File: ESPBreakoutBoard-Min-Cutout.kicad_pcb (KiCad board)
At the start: 2 copper layers, 27.5 x 32.3 mm, 15 parts, among them J1 Screw_Terminal_01x02, J2 Conn_01x09_Male, J3 Conn_01x09_Male, U1 AMS1117-3.3, U2 ESP-07

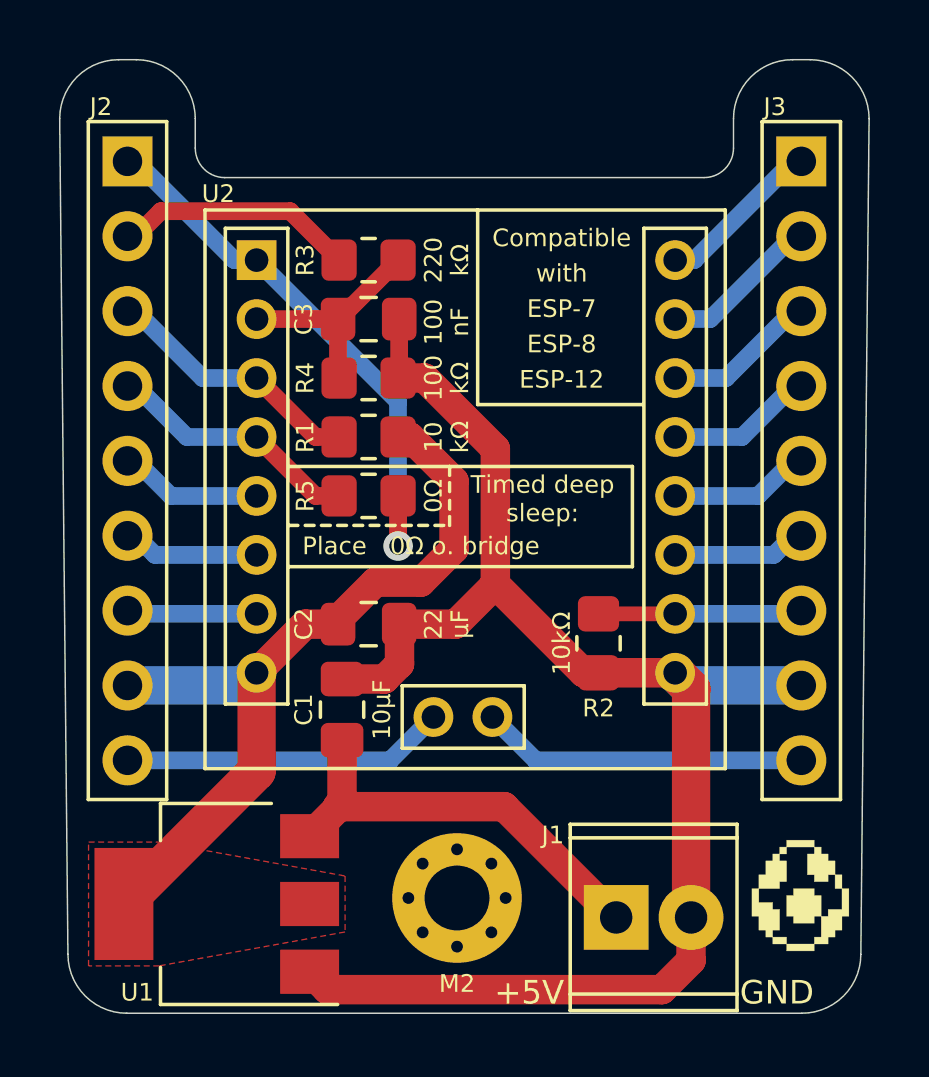
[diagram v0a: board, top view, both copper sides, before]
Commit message: v4r3: Added gerbers, fixed odd edge cuts
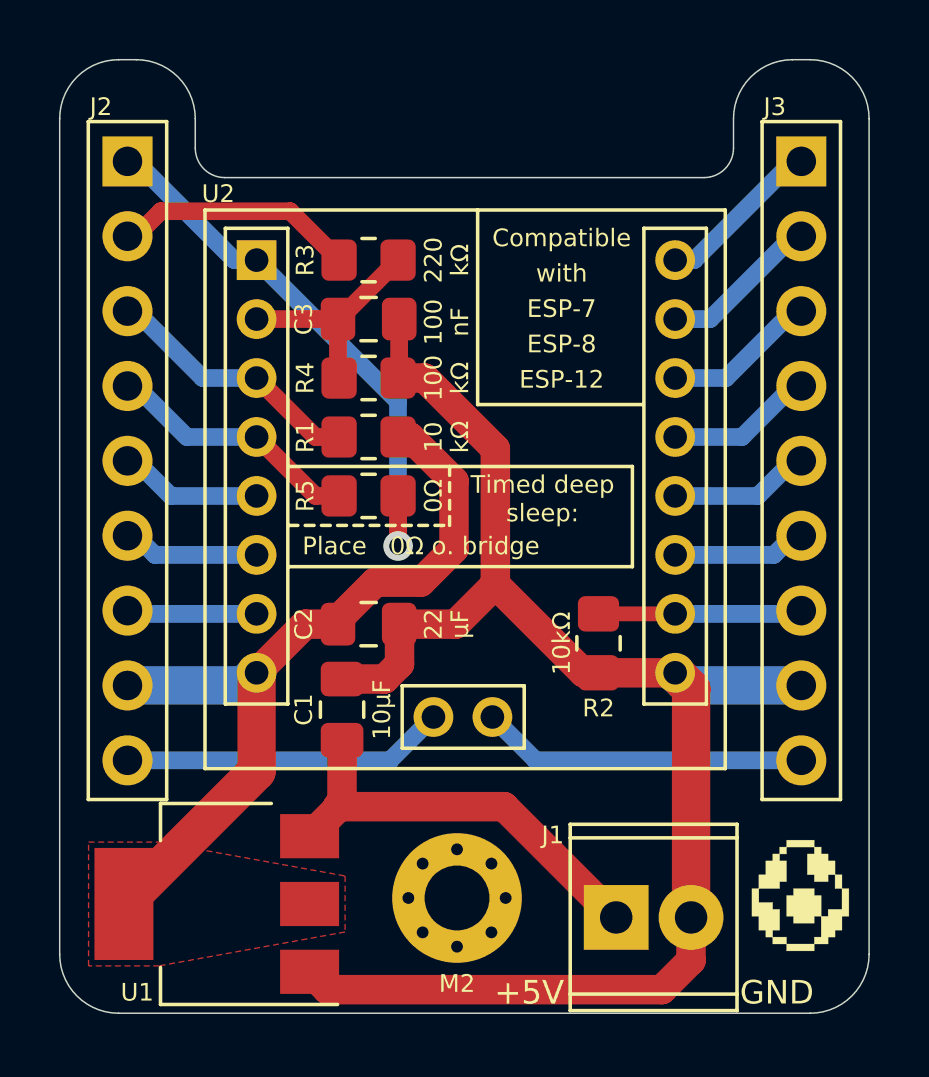
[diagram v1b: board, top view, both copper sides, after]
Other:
- outline, holes or cut-outs redrawn
- board text added: "v4r3"
- board text removed: "v4r2"
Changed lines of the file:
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@@
       (plotinvisibletext false)
       (sketchpadsonfab false)
-      (subtractmaskfromsilk true)
+      (subtractmaskfromsilk false)
       (outputformat 1)
       (mirror false)
       (drillshape 0)
       (scaleselection 1)
-      (outputdirectory "Gerbers-JLCPCB/")
+      (outputdirectory "Gerbers-PCBWay")
     )
   )
@@
   (gr_line (start 150.5 75.7) (end 156.1 75.7) (layer "F.SilkS") (width 0.12))
   (gr_line (start 155.75 81.2) (end 144.1 81.2) (layer "F.SilkS") (width 0.12))
-  (gr_line (start 136.6 94.35) (end 136.32 66) (layer "Edge.Cuts") (width 0.05))
+  (gr_line (start 136.32 94.35) (end 136.32 66) (layer "Edge.Cuts") (width 0.05))
   (gr_arc (start 138.92 64) (mid 140.334214 64.585786) (end 140.92 66) (layer "Edge.Cuts") (width 0.05))
   (gr_arc (start 159.18 66) (mid 159.765786 64.585786) (end 161.18 64) (layer "Edge.Cuts") (width 0.05))
@@
   (gr_line (start 141.92 68) (end 158.18 68) (layer "Edge.Cuts") (width 0.05))
   (gr_line (start 140.92 66) (end 140.92 67) (layer "Edge.Cuts") (width 0.05))
-  (gr_arc (start 163.5 94.35) (mid 162.914214 95.764214) (end 161.5 96.35) (layer "Edge.Cuts") (width 0.05))
+  (gr_arc (start 163.78 94.35) (mid 163.194214 95.764214) (end 161.78 96.35) (layer "Edge.Cuts") (width 0.05))
   (gr_arc (start 161.78 64) (mid 163.194214 64.585786) (end 163.78 66) (layer "Edge.Cuts") (width 0.05))
   (gr_arc (start 141.92 68) (mid 141.212893 67.707107) (end 140.92 67) (layer "Edge.Cuts") (width 0.05))
   (gr_line (start 159.18 66) (end 159.18 67) (layer "Edge.Cuts") (width 0.05))
-  (gr_arc (start 138.6 96.35) (mid 137.185786 95.764214) (end 136.6 94.35) (layer "Edge.Cuts") (width 0.05))
+  (gr_arc (start 138.32 96.35) (mid 136.905786 95.764214) (end 136.32 94.35) (layer "Edge.Cuts") (width 0.05))
   (gr_line (start 138.32 64) (end 138.92 64) (layer "Edge.Cuts") (width 0.05))
   (gr_arc (start 159.18 67) (mid 158.887107 67.707107) (end 158.18 68) (layer "Edge.Cuts") (width 0.05))
-  (gr_line (start 161.5 96.35) (end 138.6 96.35) (layer "Edge.Cuts") (width 0.05))
+  (gr_line (start 161.78 96.35) (end 138.32 96.35) (layer "Edge.Cuts") (width 0.05))
   (gr_arc (start 136.32 66) (mid 136.905786 64.585786) (end 138.32 64) (layer "Edge.Cuts") (width 0.05))
-  (gr_line (start 163.78 66) (end 163.5 94.35) (layer "Edge.Cuts") (width 0.05))
+  (gr_line (start 163.78 66) (end 163.78 94.35) (layer "Edge.Cuts") (width 0.05))
   (gr_text "JLCJLCJLCJLC" (at 142.9 95.3) (layer "B.SilkS")
     (effects (font (size 1 1) (thickness 0.15)) (justify mirror))
@@
     (effects (font (size 0.6 0.6) (thickness 0.1)) (justify mirror))
   )
-  (gr_text "v4r2" (at 145.25 81.9) (layer "B.SilkS")
+  (gr_text "v4r3" (at 145.25 81.9) (layer "B.SilkS")
     (effects (font (size 0.7 0.7) (thickness 0.13)) (justify mirror))
   )

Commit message: Added iBOM
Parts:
- renumbered G*** to G1
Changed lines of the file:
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@@
     (at 161.45 92.35)
     (attr through_hole)
-    (fp_text reference "G***" (at 0 0) (layer "F.SilkS") hide
+    (fp_text reference "G1" (at 0 0) (layer "F.SilkS") hide
       (effects (font (size 1.524 1.524) (thickness 0.3)))
     )
